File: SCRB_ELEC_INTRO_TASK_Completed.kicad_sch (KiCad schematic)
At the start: 16 parts, among them J1 Conn_01x04_Pin, U1 MCP25625-x-SS, U2 STM32G030F6Px, U3 AP2127R-3.3

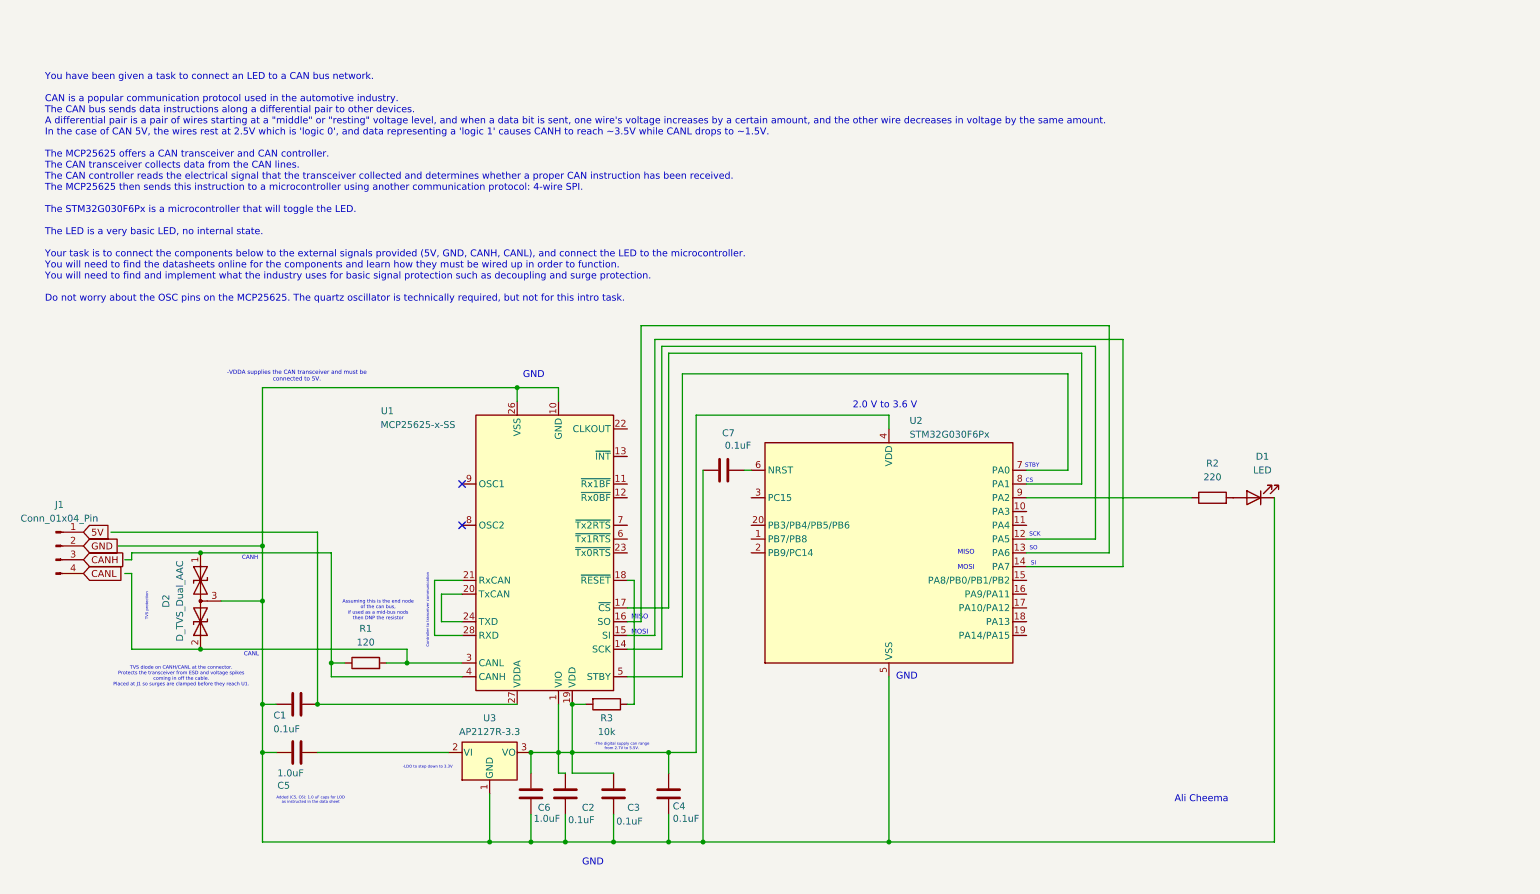
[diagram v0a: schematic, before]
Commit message: v2: net labels, edited MCP symbol for power orientation, NRST button + SWD header, J1 fixed, LED moved to PA4
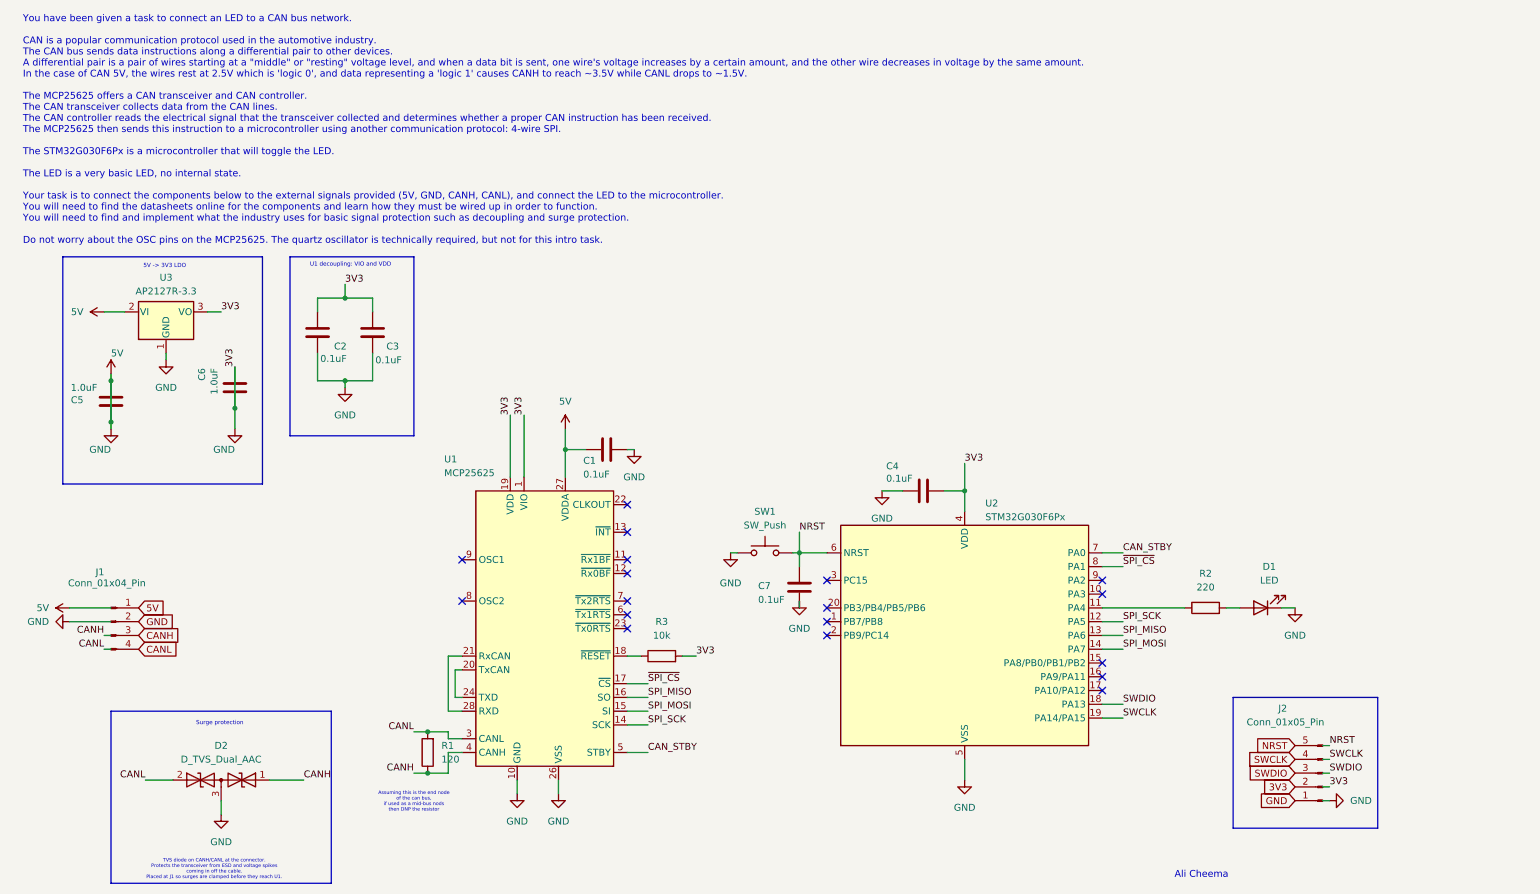
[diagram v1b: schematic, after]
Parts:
- removed U1: MCP25625-x-SS, Package_SO:SSOP-28_5.3x10.2mm_P0.65mm, symbol Interface_CAN_LIN:MCP25625-x-SS
- added J2: Conn_01x05_Pin, symbol Connector:Conn_01x05_Pin
- added SW1: SW_Push, symbol Switch:SW_Push
- added U1: MCP25625, Package_SO:SSOP-28_5.3x10.2mm_P0.65mm, symbol New_Library:MCP25625_SCRB
- C7: Name Dielectric -> (none); Value* X7R -> (none)
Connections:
- net GND is gone; now on net 5V: J1.2 (Pin_2)
- net 5V: now also C1.1, C1.2, C2.1, C2.2, C3.1, C3.2, C4.1, C4.2, C5.1, C5.2, C6.1, C6.2, C7.1, D1.1 (K), D2.3 (common), R3.2, U2.4 (VDD), U2.5 (VSS), U3.1 (GND), U3.2 (VI), U3.3 (VO), J2.1 (Pin_1), J2.2 (Pin_2), SW1.1, U1.1 (VIO), U1.10 (GND), U1.19 (VDD), U1.26 (VSS), U1.27 (VDDA)
- net CANH: now also D2.1 (A1), R1.1, U1.4 (CANH)
- net CANL: now also D2.2 (A2), R1.2, U1.3 (CANL)
- net NRST: now reaches C7.2, U2.6 (NRST)
- net NRST: now also J2.5 (Pin_5), SW1.2
- net at R3.1: now also U1.18 (~{RESET})
- net at R2.1: now also U2.11 (PA4); no longer U2.9 (PA2)
- net SPI_SCK: now reaches U2.12 (PA5)
- net SPI_SCK: now also U1.14 (SCK)
- net SPI_MOSI: now reaches U2.14 (PA7)
- net SPI_MOSI: now also U1.15 (SI)
- net SPI_MISO: now reaches U2.13 (PA6)
- net SPI_MISO: now also U1.16 (SO)
- net ~{SPI_CS}: now reaches U2.8 (PA1)
- net ~{SPI_CS}: now also U1.17 (~{CS})
- net CAN_STBY: now reaches U2.7 (PA0)
- net CAN_STBY: now also U1.5 (STBY)
- net SWDIO: now reaches U2.18 (PA13)
- net SWDIO: now also J2.3 (Pin_3)
- net SWCLK: now reaches U2.19 (PA14/PA15)
- net SWCLK: now also J2.4 (Pin_4)
- new net: U1.20 (TxCAN), U1.24 (TXD)
- new net: U1.21 (RxCAN), U1.28 (RXD)
- no-connect marks 2 -> 18
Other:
- note added: "5V -> 3V3 LDO"
- note added: "Surge protection"
- note added: "U1 decoupling: VIO and VDD"
- note removed: "-LDO to step down to 3.3V"
- note removed: "-The digital supply can range from 2.7V to 5.5V."
- note removed: "-VDDA supplies the CAN transceiver and must be connected to 5V."
- note removed: "2.0 V to 3.6 V"
- note removed: "Added (C5, C6): 1.0 uF caps for LOD as instructed in the data sheet"
- note removed: "CANH"
- note removed: "CANL"
- note removed: "CS"
- note removed: "Controller to tranceiver communication"
- note removed: "GND"
- note removed: "MISO"
- note removed: "MOSI"
- note removed: "SCK"
- note removed: "SI"
- note removed: "SO"
- note removed: "STBY"
- note removed: "TVS protection"
- moved on the sheet: C1, C2, C3, C4, C5, D1, D2, J1, R1, R2, U2, U3
